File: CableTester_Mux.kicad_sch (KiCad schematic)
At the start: 10 parts, among them J1 7-188275-8, J2 7-188275-8, J3 7-188275-8, J4 7-188275-8, J5 1787072, J6 Signal, J7 Conn_01x04_MountingPin, J8 Conn_01x04_MountingPin, U1 DG1206EUI+

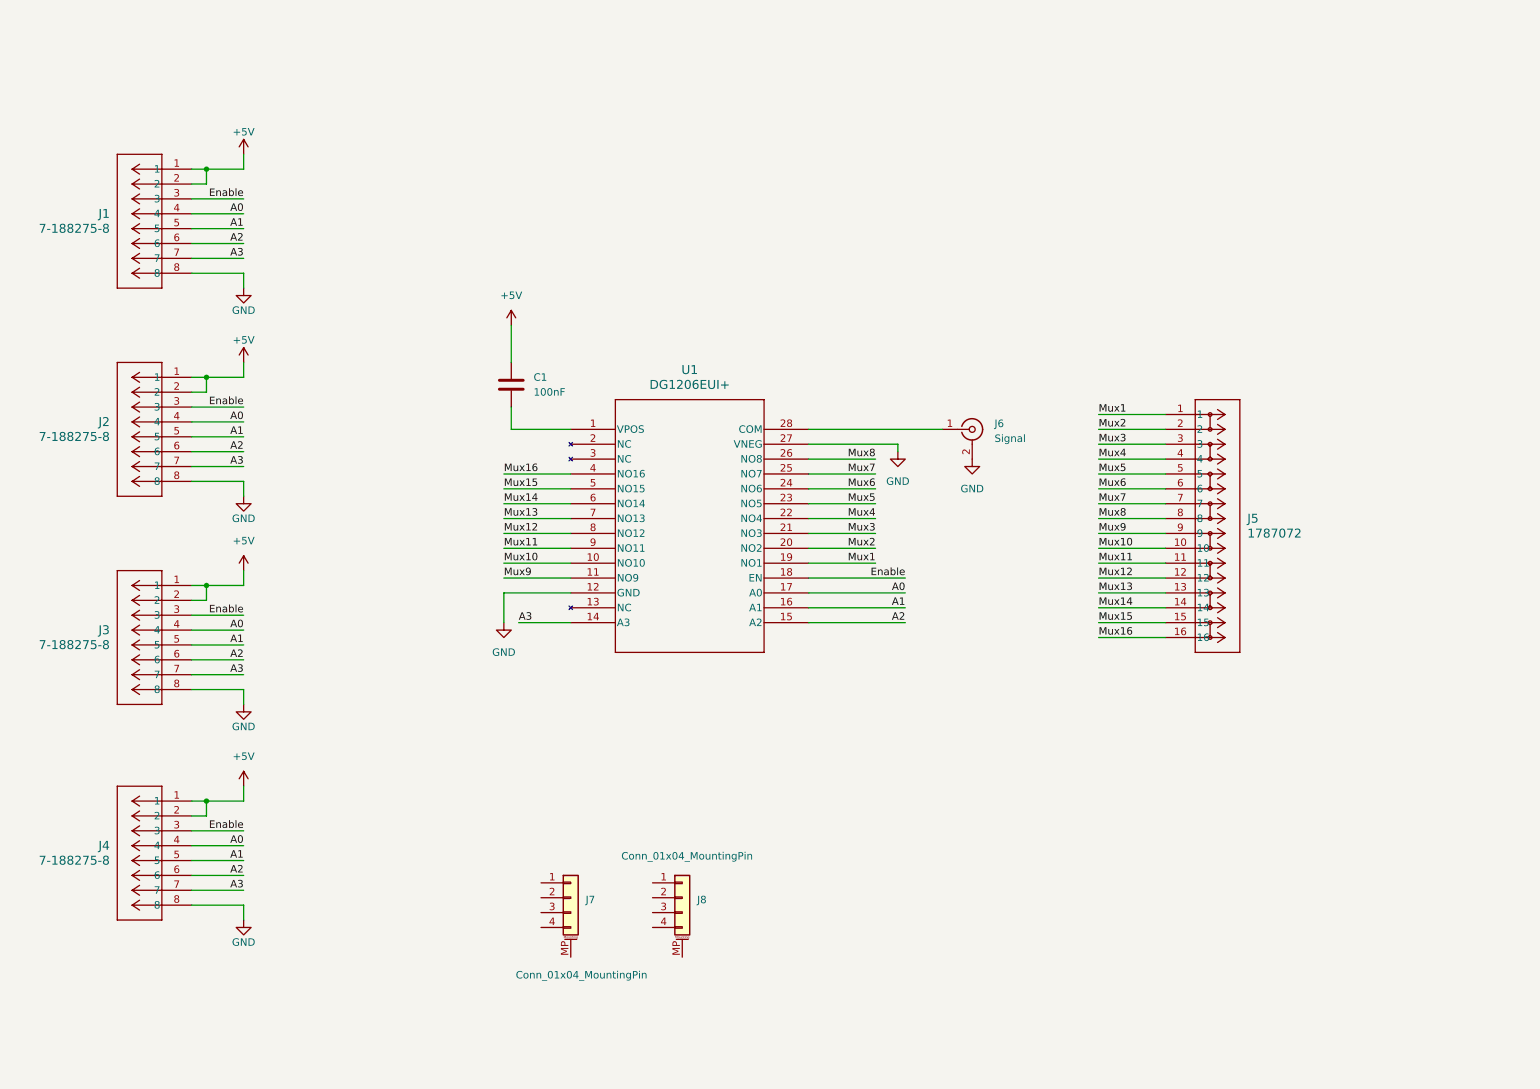
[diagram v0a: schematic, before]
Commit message: Fixed/Completed Initial Libraries
-Completed initial libraries
-Updated schematic and layout with part metadata
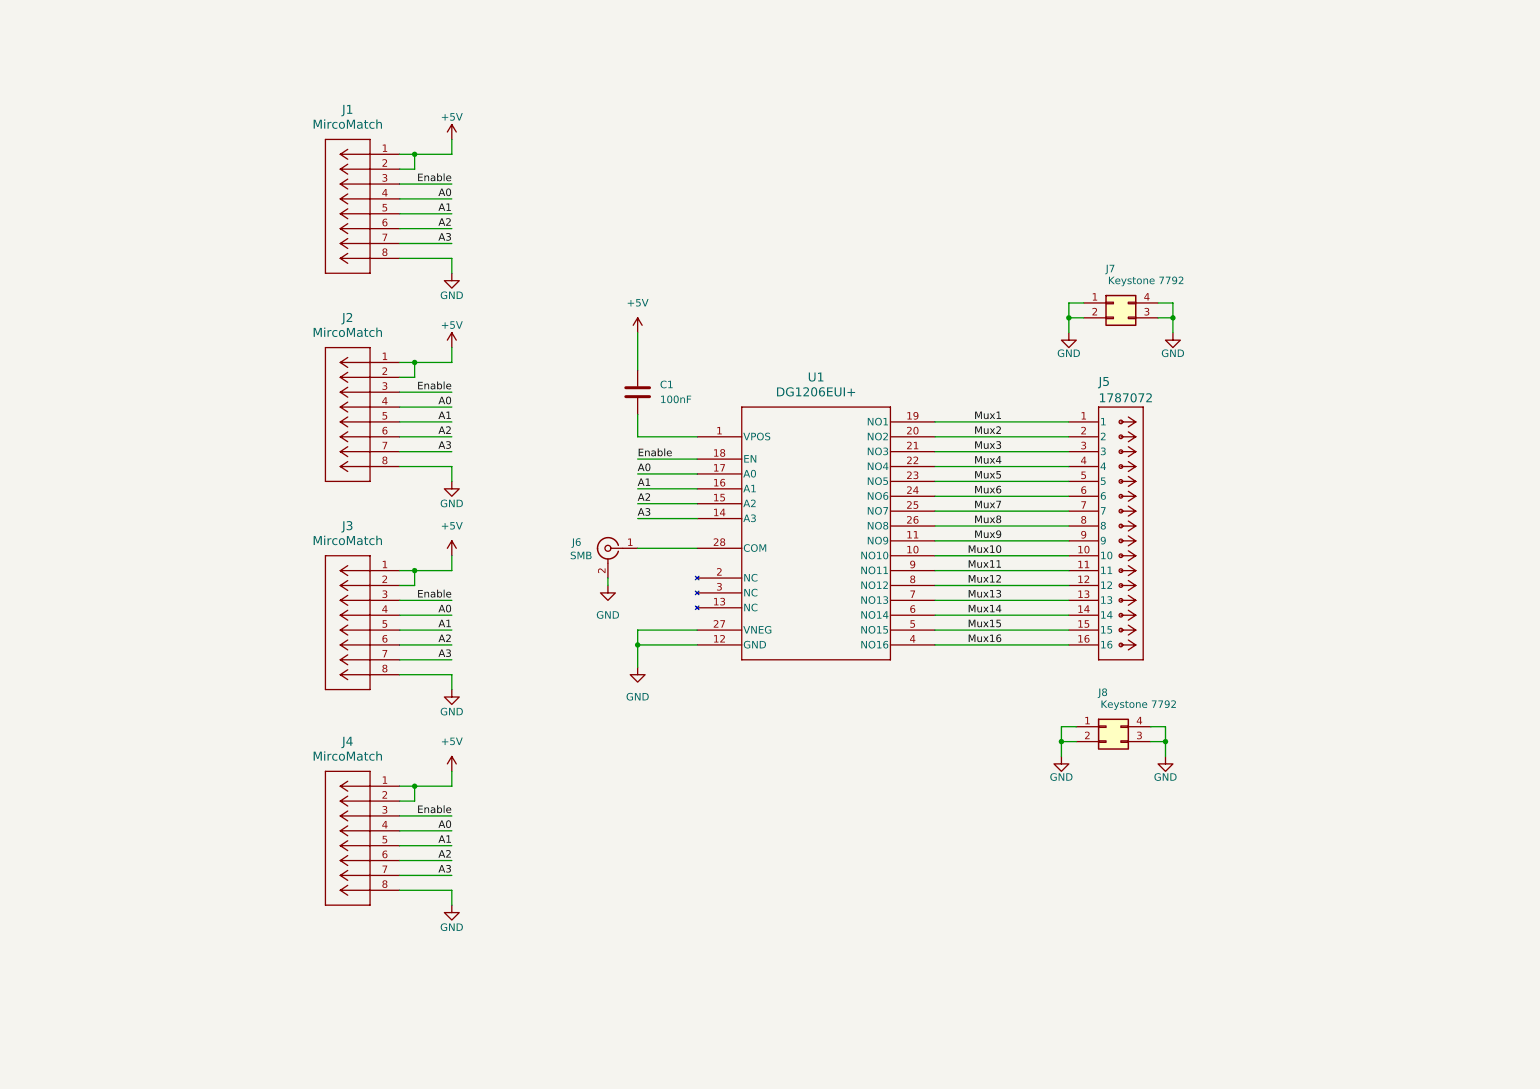
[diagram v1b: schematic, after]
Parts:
- removed J8: Conn_01x04_MountingPin, footprints:KEYSTONE_7792, symbol Connector_Generic_MountingPin:Conn_01x04_MountingPin
- removed U1: DG1206EUI+, footprints:21-0066O_U28&plus_2_MXM-M, symbol 3:DG1206EUI+
- added J8: Keystone 7792, Footprints:KEYSTONE_7792, symbol Connector_Generic:Conn_02x02_Counter_Clockwise
- added U1: DG1206EUI+, Package_SO:TSSOP-28_4.4x9.7mm_P0.65mm, symbol CableTester_Mux_Project_Lib:DG1206EUI+
- J1, J2, J3, J4: value 7-188275-8 -> MircoMatch; footprint footprints:CONN_7-188275-8_TYC -> Footprints:CONN_7-188275-8_TYC; symbol 1:7-188275-8 -> CableTester_Mux_Project_Lib:7-188275-8
- J5: footprint footprints:CONN_1787072_PXC -> Footprints:CONN_1787072_PXC; symbol 2:1787072 -> CableTester_Mux_Project_Lib:1787072
- J6: value Signal -> SMB; footprint footprints:CONN_142146_AMP -> Footprints:CONN_142146_AMP
- J7: value Conn_01x04_MountingPin -> Keystone 7792; footprint footprints:KEYSTONE_7792 -> Footprints:KEYSTONE_7792; symbol Connector_Generic_MountingPin:Conn_01x04_MountingPin -> Connector_Generic:Conn_02x02_Counter_Clockwise
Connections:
- net A0: now also U1.17 (A0)
- net A1: now also U1.16 (A1)
- net A2: now also U1.15 (A2)
- net A3: now also U1.14 (A3)
- net Enable: now also U1.18 (EN)
- net GND: now also J7.1 (Pin_1), J7.2 (Pin_2), J7.3 (Pin_3), J7.4 (Pin_4), J8.1 (Pin_1), J8.2 (Pin_2), J8.3 (Pin_3), J8.4 (Pin_4), U1.12 (GND), U1.27 (VNEG)
- net Mux1: now also U1.19 (NO1)
- net Mux10: now also U1.10 (NO10)
- net Mux11: now also U1.9 (NO11)
- net Mux12: now also U1.8 (NO12)
- net Mux13: now also U1.7 (NO13)
- net Mux14: now also U1.6 (NO14)
- net Mux15: now also U1.5 (NO15)
- net Mux16: now also U1.4 (NO16)
- net Mux2: now also U1.20 (NO2)
- net Mux3: now also U1.21 (NO3)
- net Mux4: now also U1.22 (NO4)
- net Mux5: now also U1.23 (NO5)
- net Mux6: now also U1.24 (NO6)
- net Mux7: now also U1.25 (NO7)
- net Mux8: now also U1.26 (NO8)
- net Mux9: now also U1.11 (NO9)
- net at C1.2: now also U1.1 (VPOS)
- net at J6.1 (In): now also U1.28 (COM)
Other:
- company: (none) -> LBNL - ALSU
- title: (none) -> CableTester Mux Breakout
- moved on the sheet: C1, J6

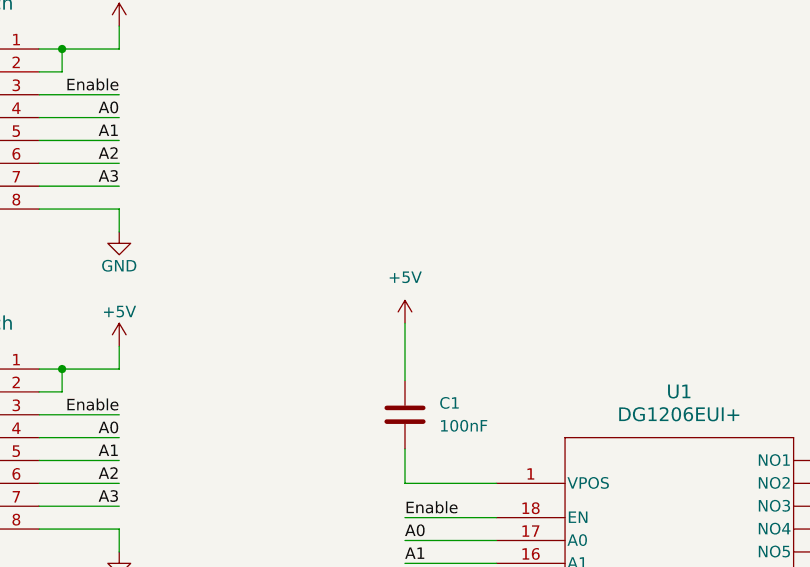
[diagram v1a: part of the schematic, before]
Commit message: updated lib links and metadata
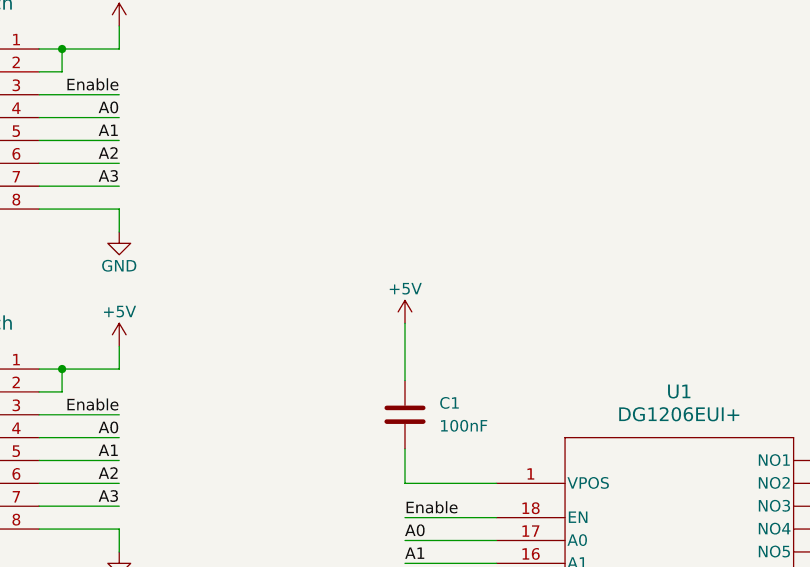
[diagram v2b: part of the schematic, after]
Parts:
- J6: symbol Connector:Conn_Coaxial -> CableTester_Mux_Project_Lib:Conn_Coaxial
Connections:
- net GND: now also J6.3 (Ext), J6.4 (Ext), J6.5 (Ext)
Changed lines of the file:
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@@
 	)
 	(symbol
-		(lib_id "Connector:Conn_Coaxial")
+		(lib_id "power:+5V")
+		(at 125.73 68.58 0)
+		(unit 1)
+		(exclude_from_sim no)
+		(in_bom yes)
+		(on_board yes)
+		(dnp no)
+		(property "Reference" "#PWR01"
+			(at 125.73 72.39 0)
+			(effects
+				(font
+					(size 1.27 1.27)
+				)
+				(hide yes)
+			)
+		)
+		(property "Value" "+5V"
+			(at 125.73 64.77 0)
+			(effects
+				(font
+					(size 1.27 1.27)
+				)
+			)
+		)
+		(property "Footprint" ""
+			(at 125.73 68.58 0)
+			(effects
+				(font
+					(size 1.27 1.27)
+				)
+				(hide yes)
+			)
+		)
+		(property "Datasheet" ""
+			(at 125.73 68.58 0)
+			(effects
+				(font
+					(size 1.27 1.27)
+				)
+				(hide yes)
+			)
+		)
+		(property "Description" "Power symbol creates a global label with name \"+5V\""
+			(at 125.73 68.58 0)
+			(effects
+				(font
+					(size 1.27 1.27)
+				)
+				(hide yes)
+			)
+		)
+		(pin "1"
+		)
+		(instances
+			(project "CableTester_Mux"
+				(path "/841f615f-04b3-41d5-a150-d938aabba9aa"
+					(reference "#PWR01")
+					(unit 1)
+				)
+			)
+		)
+	)
+	(symbol
+		(lib_id "CableTester_Mux_Project_Lib:Conn_Coaxial")
 		(at 120.65 105.41 0)
 		(mirror y)
@@
 		)
 		(pin "2"
+		)
+		(pin "4"
+		)
+		(pin "5"
+		)
+		(pin "3"
 		)
 		(instances
@@
 					(unit 1)
 				)
-			)
-		)
-	)
-	(symbol
-		(lib_id "power:+5V")
-		(at 125.73 68.58 0)
-		(unit 1)
-		(exclude_from_sim no)
-		(in_bom yes)
-		(on_board yes)
-		(dnp no)
-		(fields_autoplaced yes)
-		(property "Reference" "#PWR01"
-			(at 125.73 72.39 0)
-			(effects
-				(font
-					(size 1.27 1.27)
-				)
-				(hide yes)
-			)
-		)
-		(property "Value" "+5V"
-			(at 125.73 63.5 0)
-			(effects
-				(font
-					(size 1.27 1.27)
-				)
-			)
-		)
-		(property "Footprint" ""
-			(at 125.73 68.58 0)
-			(effects
-				(font
-					(size 1.27 1.27)
-				)
-				(hide yes)
-			)
-		)
-		(property "Datasheet" ""
-			(at 125.73 68.58 0)
-			(effects
-				(font
-					(size 1.27 1.27)
-				)
-				(hide yes)
-			)
-		)
-		(property "Description" "Power symbol creates a global label with name \"+5V\""
-			(at 125.73 68.58 0)
-			(effects
-				(font
-					(size 1.27 1.27)
-				)
-				(hide yes)
-			)
-		)
-		(pin "1"
-		)
-		(instances
-			(project ""
-				(path "/841f615f-04b3-41d5-a150-d938aabba9aa"
-					(reference "#PWR01")
-					(unit 1)
-				)

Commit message: Added filtering components for AC coupled UART to schematic
Added DC blocking cap and DC re-biasing resistors to schematic.
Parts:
- added C10, C11, C12, C13, C14, C15, C16, C17, C2, C3, C4, C5, C6, C7, C8, C9: 10uF, Capacitor_SMD:C_1210_3225Metric_Pad1.33x2.70mm_HandSolder, symbol Device:C_Small
- added R1, R10, R11, R12, R13, R14, R15, R16, R17, R18, R19, R2, R20, R21, R22, R23, R24, R25, R26, R27, R28, R29, R3, R30, R31, R32, R4, R5, R6, R7, R8, R9: 100k, Resistor_SMD:R_0603_1608Metric_Pad0.98x0.95mm_HandSolder, symbol Device:R_Small_US
- added R33, R34, R35, R36, R37, R38, R39, R40, R41, R42, R43, R44, R45, R46, R47, R48, R49, R50: 0R, Resistor_SMD:R_0603_1608Metric_Pad0.98x0.95mm_HandSolder, symbol Device:R_Small_US
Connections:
- net +5V: now also C1.2, U1.1 (VPOS); no longer C1.1, J1.2, J2.2, J3.2, J4.2
- net GND: now also C1.1
- net Mux1: no longer J5.1
- net Mux10: no longer J5.10
- net Mux11: no longer J5.11
- net Mux12: no longer J5.12
- net Mux13: no longer J5.13
- net Mux14: no longer J5.14
- net Mux15: no longer J5.15
- net Mux16: no longer J5.16
- net Mux2: no longer J5.2
- net Mux3: no longer J5.3
- net Mux4: no longer J5.4
- net Mux5: no longer J5.5
- net Mux6: no longer J5.6
- net Mux7: no longer J5.7
- net Mux8: no longer J5.8
- net Mux9: no longer J5.9
- new net +3.3V: J1.2, J2.2, J3.2, J4.2
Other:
- moved on the sheet: C1, J5, J7, J8
